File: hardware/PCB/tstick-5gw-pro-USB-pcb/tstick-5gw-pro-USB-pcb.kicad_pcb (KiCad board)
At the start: 4 copper layers, 76.8 x 96.8 mm, 52 parts, among them J1 USB_C_Receptacle_USB2.0, J2 GPIO2, J3 GPIO1, Q2 20V/4.2A/52mOhm/1.4W, Q3 BSS138, SW1 JST-SH-1.00mm 1x2, SW2 PTS810 SJM Switch, U1 XC6222B331MR-G, U3 MCP73831-2-OT, U4 PCA9306DP

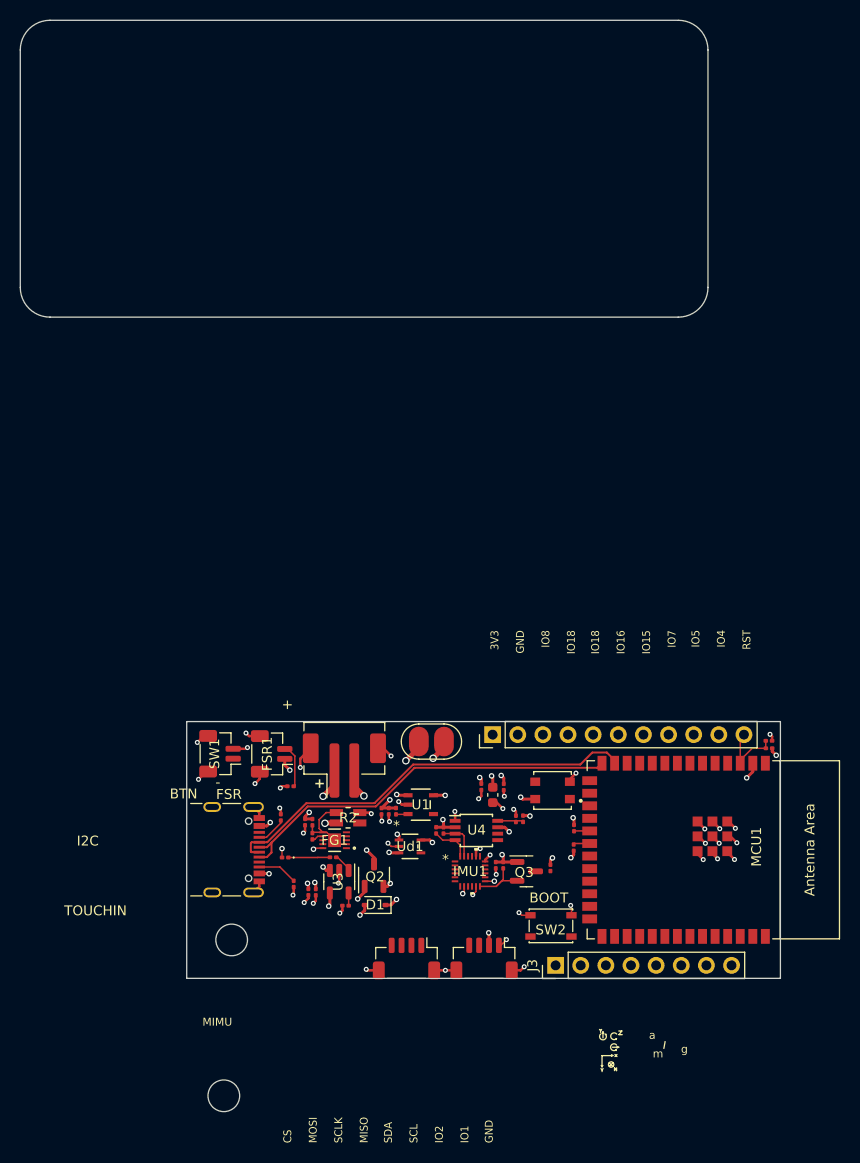
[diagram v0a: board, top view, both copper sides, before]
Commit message: completed usb only design
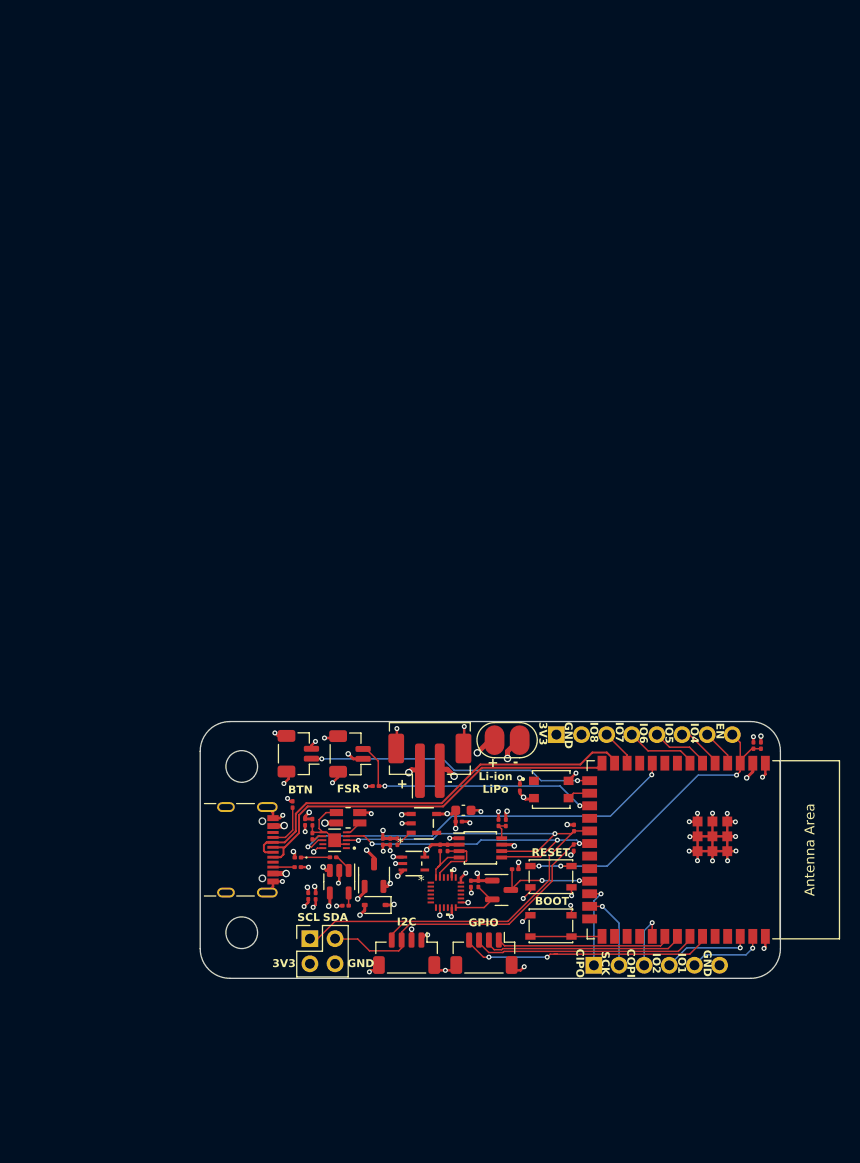
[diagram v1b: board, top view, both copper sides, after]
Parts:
- added I2C2: Conn_01x04, Connector_PinHeader_2.54mm:PinHeader_2x02_P2.54mm_Vertical, F.Cu at (110.1, 69.3)
- added SW3: PTS810 SJM Switch, Button_Switch_SMD:SW_SPST_PTS810, F.Cu at (134.5, 63.0)
- J2: footprint Connector_PinHeader_2.54mm:PinHeader_1x11_P2.54mm_Vertical -> Connector_PinHeader_2.54mm:PinHeader_1x08_P2.54mm_Vertical
- J3: footprint Connector_PinHeader_2.54mm:PinHeader_1x08_P2.54mm_Vertical -> Connector_PinHeader_2.54mm:PinHeader_1x06_P2.54mm_Vertical
- moved H1 33.3 mm to (103.2, 51.9)
- moved BT1 8.64 mm to (122.2, 51.8)
- moved R1 8.62 mm to (116.8, 53.9)
- moved FSR1 7.92 mm to (114.2, 50.6)
- moved SW1 7.92 mm to (108.9, 50.6)
- moved TrillExtensionInput1 7.85 mm to (127.7, 70.8)
- moved QWIIC1 7.85 mm to (119.9, 70.8)
- moved BT2 7.65 mm to (128.8, 49.2)
- moved J2 6.44 mm to (135.0, 48.7)
- moved C7 4.18 mm to (125.2, 57.5), turned to 0 degrees
- moved J3 3.87 mm to (138.8, 72.0)
- moved R23 3.56 mm to (130.8, 62.3), turned to 0 degrees
- moved C8 3.35 mm to (125.6, 56.3), turned to 0 degrees
- moved IMU1 3.25 mm to (123.8, 64.6)
- moved Q3 3.14 mm to (129.5, 64.4)
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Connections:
- J2 pad 4: /IO18 -> /IO7
- J2 pad 5: /IO16 -> /IO6
- J2 pad 6: /IO15 -> /IO5
- J2 pad 7: /IO7 -> /IO4
- J2 pad 8: /IO6 -> /EN
- J3 pad 1: /SCL -> /CIPO
- J3 pad 2: /SDA -> /SCK
- J3 pad 3: /CIPO -> /COPI
- J3 pad 4: /SCK -> /IO2
- J3 pad 5: /COPI -> /IO1
- J3 pad 6: /IO2 -> GND
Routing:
- net /SCL: track 1.59 -> 65.2 mm, vias 0 -> 2
- net /SDA: track 1.65 -> 62.1 mm, vias 0 -> 3
- net /IO17: track 0.00 -> 40.7 mm, vias 0 -> 2
- net /IO3: track 0.00 -> 29.0 mm, vias 0 -> 2
- net /EN: track 7.20 -> 33.9 mm, vias 0 -> 3
- net /IO42: track 0.00 -> 26.0 mm, vias 0 -> 2
- net /IO41: track 0.00 -> 22.9 mm
- net /IO9: track 4.42 -> 26.7 mm, vias 0 -> 2
- net GND: track 53.9 -> 75.0 mm, vias 46 -> 54
- net /IO40: track 0.00 -> 20.4 mm
- net /IO39: track 0.00 -> 17.7 mm
- net /IO21: track 0.00 -> 10.5 mm, vias 0 -> 2
- net /IO2: track 0.00 -> 9.06 mm, vias 0 -> 1
- net /CIPO: track 0.00 -> 8.67 mm, vias 0 -> 1
- net /SCK: track 0.00 -> 7.93 mm, vias 0 -> 1
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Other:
- board size 76.8 x 96.8 mm -> 58.6 x 26 mm
- board text added: "3V3"
- board text added: "ANALOG/ BTN IN IO3"
- board text added: "Custom T-Stick Board v0.0.2 2023-09 IDMIL McGill University"
- board text added: "EN IO4 IO5 IO6"
- board text added: "EVT1 = IO39 EVT2 = IO40 EVT3 = IO41 EVT4 = IO42"
- board text added: "FSR IN IO9"
- board text added: "GND IO1 IO2 COPI SCK CIPO"
- board text added: "GPIO"
- board text added: "IO7 IO8 GND 3V3"
- board text added: "Li-ion LiPo"
- board text added: "MIMU ORIENTATION"
- board text added: "RESET"
- board text added: "SCL"
- board text added: "SCL = IO11 SDA = IO12 STATUS LED = IO46 IMU INT = IO21 FUEL GAUGE INT = IO17"
- board text added: "SDA"
- board text added: "n"
- board text added: "x"
- board text added: "y"
- board text added: "z"
- board text removed: "3V3 GND IO8 IO18"
- board text removed: "Albert Niyonsenga 2023-09-05"
- board text removed: "CS MOSI SCLK MISO"
- board text removed: "Custom T-Stick Board v0.0.1 2023-09-05 IDMIL McGill University"
- board text removed: "EVT1 = IO11 EVT2 = IO12 EVT3 = IO13 EVT4 = IO14"
- board text removed: "IO10/CS IO11/MOSI IO12/SCLK IO13/MISO"
- board text removed: "IO18 IO16 IO15 IO7"
- board text removed: "IO5 IO4 RST"
- board text removed: "MIMU"
- board text removed: "SDA SCL IO2 IO1"
- board text removed: "TOUCHIN"

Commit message: minor schematic adjustments
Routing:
- net GND: track 75.0 -> 73.3 mm

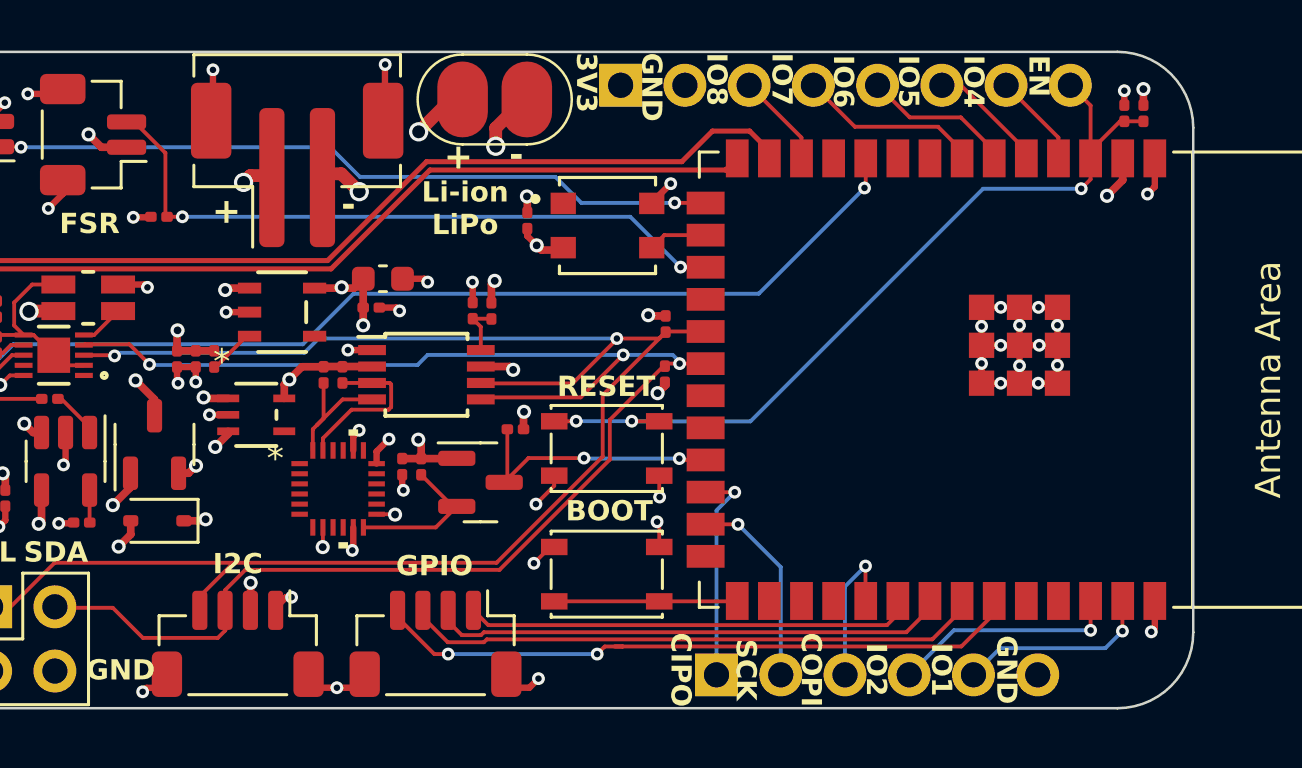
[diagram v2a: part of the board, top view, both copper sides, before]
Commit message: updated BOM for 5gw board, updated silkscreen for touch board
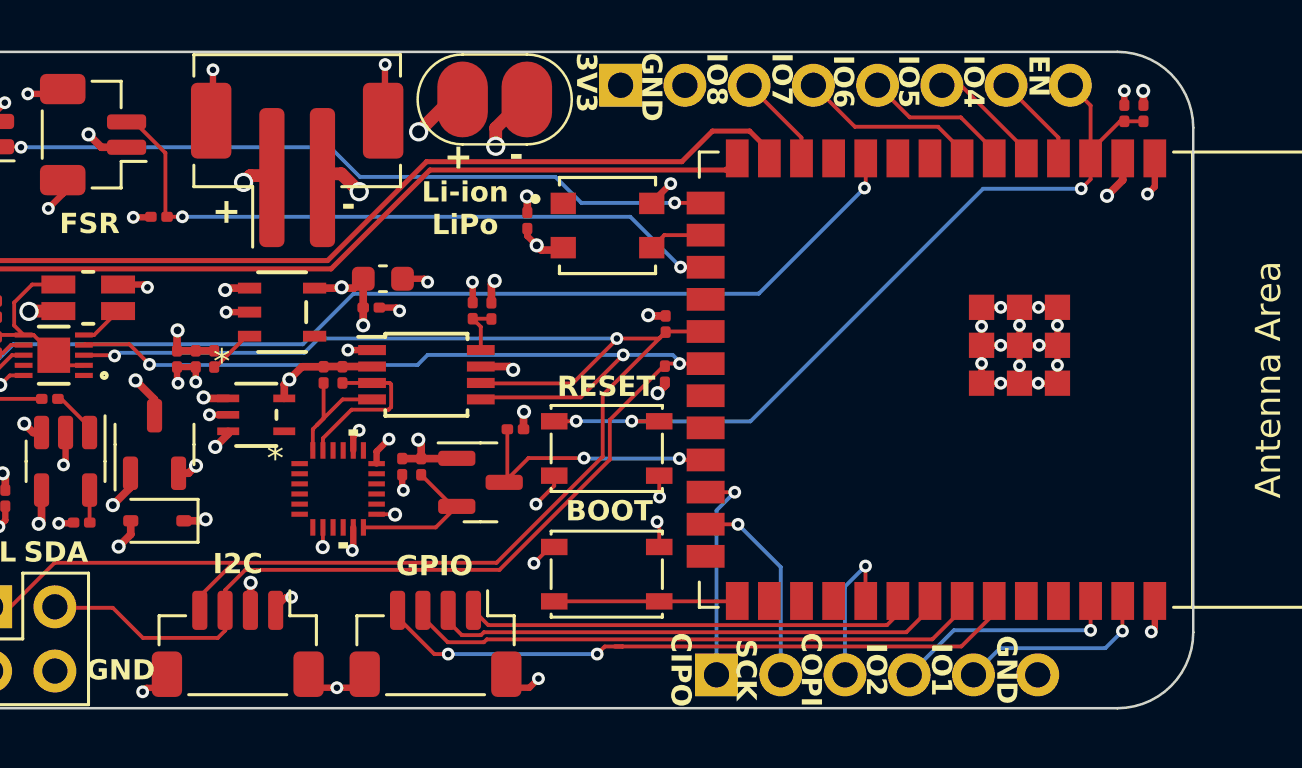
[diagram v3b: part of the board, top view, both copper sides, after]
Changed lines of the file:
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@@
     (pad "4" smd roundrect (at 1.5 1.325 180) (size 0.6 1.55) (layers "F.Cu" "F.Paste" "F.Mask") (roundrect_rratio 0.25)
       (net 11 "/SCL") (pinfunction "Pin_4") (pintype "passive"))
-    (pad "MP" smd roundrect (at -2.8 -1.2 180) (size 1.2 1.8) (layers "F.Cu" "F.Paste" "F.Mask") (roundrect_rratio 0.208333)
+    (pad "MP" smd roundrect (at -2.8 -1.2 180) (size 1.2 1.8) (layers "F.Cu" "F.Paste" "F.Mask") (roundrect_rratio 0.2083333333)
       (net 6 "GND") (pinfunction "MountPin") (pintype "passive"))
-    (pad "MP" smd roundrect (at 2.8 -1.2 180) (size 1.2 1.8) (layers "F.Cu" "F.Paste" "F.Mask") (roundrect_rratio 0.208333)
+    (pad "MP" smd roundrect (at 2.8 -1.2 180) (size 1.2 1.8) (layers "F.Cu" "F.Paste" "F.Mask") (roundrect_rratio 0.2083333333)
       (net 6 "GND") (pinfunction "MountPin") (pintype "passive"))
     (model "${KIPRJMOD}/Libraries/JST Connectors/BM04B-SRSS-TB-LF--SN---3DModel-STEP-56544.STEP"
@@
     (pad "4" smd roundrect (at 1.5 1.325 180) (size 0.6 1.55) (layers "F.Cu" "F.Paste" "F.Mask") (roundrect_rratio 0.25)
       (net 80 "/IO42") (pinfunction "Pin_4") (pintype "passive"))
-    (pad "MP" smd roundrect (at -2.8 -1.2 180) (size 1.2 1.8) (layers "F.Cu" "F.Paste" "F.Mask") (roundrect_rratio 0.208333)
+    (pad "MP" smd roundrect (at -2.8 -1.2 180) (size 1.2 1.8) (layers "F.Cu" "F.Paste" "F.Mask") (roundrect_rratio 0.2083333333)
       (net 6 "GND") (pinfunction "MountPin") (pintype "passive"))
-    (pad "MP" smd roundrect (at 2.8 -1.2 180) (size 1.2 1.8) (layers "F.Cu" "F.Paste" "F.Mask") (roundrect_rratio 0.208333)
+    (pad "MP" smd roundrect (at 2.8 -1.2 180) (size 1.2 1.8) (layers "F.Cu" "F.Paste" "F.Mask") (roundrect_rratio 0.2083333333)
       (net 6 "GND") (pinfunction "MountPin") (pintype "passive"))
     (model "${KIPRJMOD}/Libraries/JST Connectors/BM04B-SRSS-TB-LF--SN---3DModel-STEP-56544.STEP"
@@
   (segment (start 123.946748 56.689998) (end 123.978374 56.658372) (width 0.3048) (layer "F.Cu") (net 5))
   (segment (start 131.32 53.08) (end 131.32 53.7) (width 0.3048) (layer "F.Cu") (net 5))
+  (segment (start 155.67 48.89) (end 155.68 48.9) (width 0.3048) (layer "F.Cu") (net 5))
+  (segment (start 155.68 48.9) (end 155.68 49.455) (width 0.3048) (layer "F.Cu") (net 5))
   (segment (start 154.86 52.42) (end 154.24 53.04) (width 0.3048) (layer "F.Cu") (net 5))
   (segment (start 129.9 56.5325) (end 130.03 56.4025) (width 0.3048) (layer "F.Cu") (net 5))
   (segment (start 130.63 59.79) (end 130.76 59.92) (width 0.3048) (layer "F.Cu") (net 5))
   (segment (start 114.4775 51.12) (end 115.475 51.12) (width 0.3048) (layer "F.Cu") (net 5))
-  (segment (start 155.68 48.82) (end 155.68 49.455) (width 0.3048) (layer "F.Cu") (net 5))
   (segment (start 123.89 56.689998) (end 123.946748 56.689998) (width 0.3048) (layer "F.Cu") (net 5))
   (segment (start 136.4695 60.844002) (end 136.76 60.553502) (width 0.3048) (layer "F.Cu") (net 5))
@@
   (via (at 130.03 56.4025) (size 0.5588) (drill 0.3048) (layers "F.Cu" "B.Cu") (net 5))
   (via (at 131.19 61.58) (size 0.5588) (drill 0.3048) (layers "F.Cu" "B.Cu") (net 5))
-  (via (at 155.68 48.82) (size 0.5588) (drill 0.3048) (layers "F.Cu" "B.Cu") (net 5))
+  (via (at 155.67 48.89) (size 0.5588) (drill 0.3048) (layers "F.Cu" "B.Cu") (net 5))
   (via (at 136.99 52.56) (size 0.508) (drill 0.254) (layers "F.Cu" "B.Cu") (net 5))
   (via (at 123.978374 56.658372) (size 0.5588) (drill 0.3048) (layers "F.Cu" "B.Cu") (net 5))
